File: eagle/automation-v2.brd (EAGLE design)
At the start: 65.8 x 104.1 mm, 96 parts, among them IC1 MEGA48/88/168-AU, IC2 DS2482-100S, IC3 DS2482-100S, IC4 78L33, K1 SRD-05VDC-SL-C, K2 SRD-05VDC-SL-C, K3 SRD-05VDC-SL-C, K4 SRD-05VDC-SL-C, Q1 BSS123, Q2 BSS123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

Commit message: Initial PCB trace
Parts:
- added C19, C20, C21: (no value), rcl:E5-10,5
- added R37, R38, R39: (no value), rcl:M1206
- JP2, JP3: device pinhead:1X02/90 -> pinhead:1X02
- moved JP1 31.5 mm to (6.35, 17.8)
- moved R8 30.8 mm to (5.71, 12.7)
- moved JP2 24.9 mm to (4.76, -4.45), turned to 180 degrees
- moved R23 23.4 mm to (30.5, 17.8), flipped to the top
- moved R18 23.4 mm to (41.6, -23.8), flipped to the bottom
- moved JP3 21.8 mm to (4.76, -8.89), turned to 180 degrees
- moved R22 21.1 mm to (28.6, 17.8), flipped to the top
- moved R21 21.0 mm to (23.2, -35.2), flipped to the bottom, turned to 0 degrees
- moved R36 20.3 mm to (12.7, -1.91), flipped to the bottom, turned to 270 degrees
- moved R24 19.9 mm to (41.6, -42.9), flipped to the bottom
- moved R27 19.0 mm to (23.2, -17.1), flipped to the bottom, turned to 0 degrees
- moved D2 18.4 mm to (41.6, -45.4), turned to 0 degrees
- moved D1 18.1 mm to (41.9, -26.4), turned to 0 degrees
- moved R16 17.2 mm to (47.0, -19.1), turned to 180 degrees
- moved R9 16.6 mm to (46.7, -38.1), turned to 180 degrees
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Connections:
- new net N$14: C19.+, K3.A2, R37.2
- new net N$63: C20.+, K2.A2, R38.1
- new net N$66: C21.+, K1.A2, R39.1
- net 12V: now also R37.1, R38.2, R39.2; no longer K1.A2, K2.A2, K3.A2
- net GND: now also C19.-, C20.-, C21.-
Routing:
- net 12V: track 0.00 -> 296.1 mm, vias 0 -> 5
- net GND: track 0.00 -> 218.0 mm, vias 0 -> 30
- net N$46: track 0.00 -> 131.9 mm, vias 0 -> 5
- net N$23: track 0.00 -> 115.9 mm, vias 0 -> 5
- net N$53: track 0.00 -> 109.7 mm, vias 0 -> 5
- net VDD: track 0.00 -> 86.0 mm, vias 0 -> 1
- net Z5V: track 0.00 -> 79.9 mm, vias 0 -> 2
- net N$24: track 0.00 -> 78.7 mm, vias 0 -> 3
- net N$2: track 0.00 -> 70.6 mm, vias 0 -> 3
- net N$12: track 0.00 -> 66.2 mm, vias 0 -> 2
- net N$13: track 0.00 -> 53.5 mm, vias 0 -> 3
- net VCC: track 0.00 -> 51.8 mm, vias 0 -> 2
- net N$1: track 0.00 -> 48.2 mm, vias 0 -> 3
- net N$14: track 0.00 -> 47.2 mm, vias 0 -> 2
- net N$40: track 0.00 -> 45.5 mm, vias 0 -> 2
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- added copper zone on layer 1, net GND
- added copper zone on layer 16, net GND
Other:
- board size 65.8 x 104.1 mm -> 67 x 104.4 mm

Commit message: updated PCB trace
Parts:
- moved R19 54.6 mm to (30.2, 12.7), flipped to the top, turned to 90 degrees
- moved R15 53.8 mm to (39.7, 12.7), flipped to the top, turned to 270 degrees
- moved R20 51.4 mm to (28.3, 12.7), flipped to the top, turned to 270 degrees
- moved R9 51.1 mm to (41.6, 12.7), flipped to the top, turned to 90 degrees
- moved D2 48.6 mm to (40.6, 3.17), flipped to the top, turned to 90 degrees
- moved Q3 47.3 mm to (29.2, 7.62), flipped to the top, turned to 180 degrees
- moved Q1 47.0 mm to (40.6, 7.62), flipped to the top, turned to 180 degrees
- moved R25 37.5 mm to (34.0, 12.7), flipped to the top, turned to 90 degrees
- moved D3 37.0 mm to (29.2, 3.17), flipped to the top, turned to 90 degrees
- moved R17 36.0 mm to (35.9, 12.7), flipped to the top, turned to 270 degrees
- moved R26 34.4 mm to (32.1, 12.7), flipped to the top, turned to 270 degrees
- moved R16 33.1 mm to (37.8, 12.7), flipped to the top, turned to 90 degrees
- moved D1 30.0 mm to (36.8, 3.17), flipped to the top, turned to 90 degrees
- moved Q4 29.6 mm to (33.0, 7.62), flipped to the top, turned to 180 degrees
- moved Q2 28.3 mm to (36.8, 7.62), flipped to the top, turned to 180 degrees
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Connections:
- net N$23: now also IC1.14; no longer IC1.11
- net N$24: now also IC1.13; no longer IC1.12
- net N$46: now also IC1.11; no longer IC1.13
- net N$53: now also IC1.12; no longer IC1.14
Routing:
- net GND: track 218.0 -> 0.00 mm, vias 30 -> 16
- net N$46: track 131.9 -> 10.9 mm, vias 5 -> 0
- net N$23: track 115.9 -> 16.9 mm, vias 5 -> 0
- net N$53: track 109.7 -> 11.1 mm, vias 5 -> 0
- net N$41: track 9.35 -> 83.9 mm
- net 12V: track 296.1 -> 223.4 mm, vias 5 -> 4
- net N$24: track 78.7 -> 14.0 mm, vias 3 -> 0
- net N$48: track 9.38 -> 69.2 mm, vias 0 -> 1
- net N$35: track 9.54 -> 52.4 mm, vias 0 -> 1
- net N$55: track 9.34 -> 45.3 mm, vias 0 -> 1
- net VDD: track 86.0 -> 57.7 mm, vias 1 -> 2
- net N$12: track 66.2 -> 43.4 mm, vias 2 -> 1
- net N$36: track 25.6 -> 3.18 mm, vias 3 -> 1
- net N$56: track 23.1 -> 3.18 mm
- net N$43: track 23.0 -> 3.18 mm
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
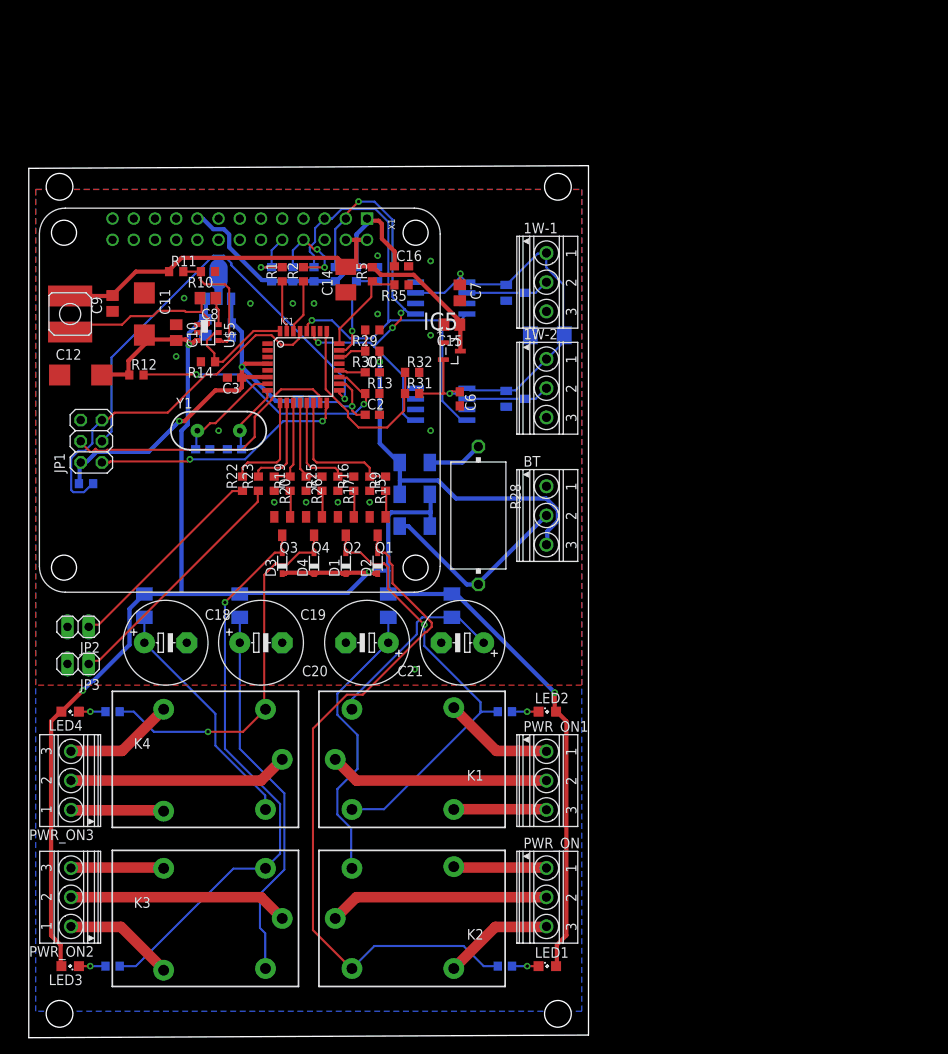
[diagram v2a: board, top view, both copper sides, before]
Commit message: RC version of PCB trace
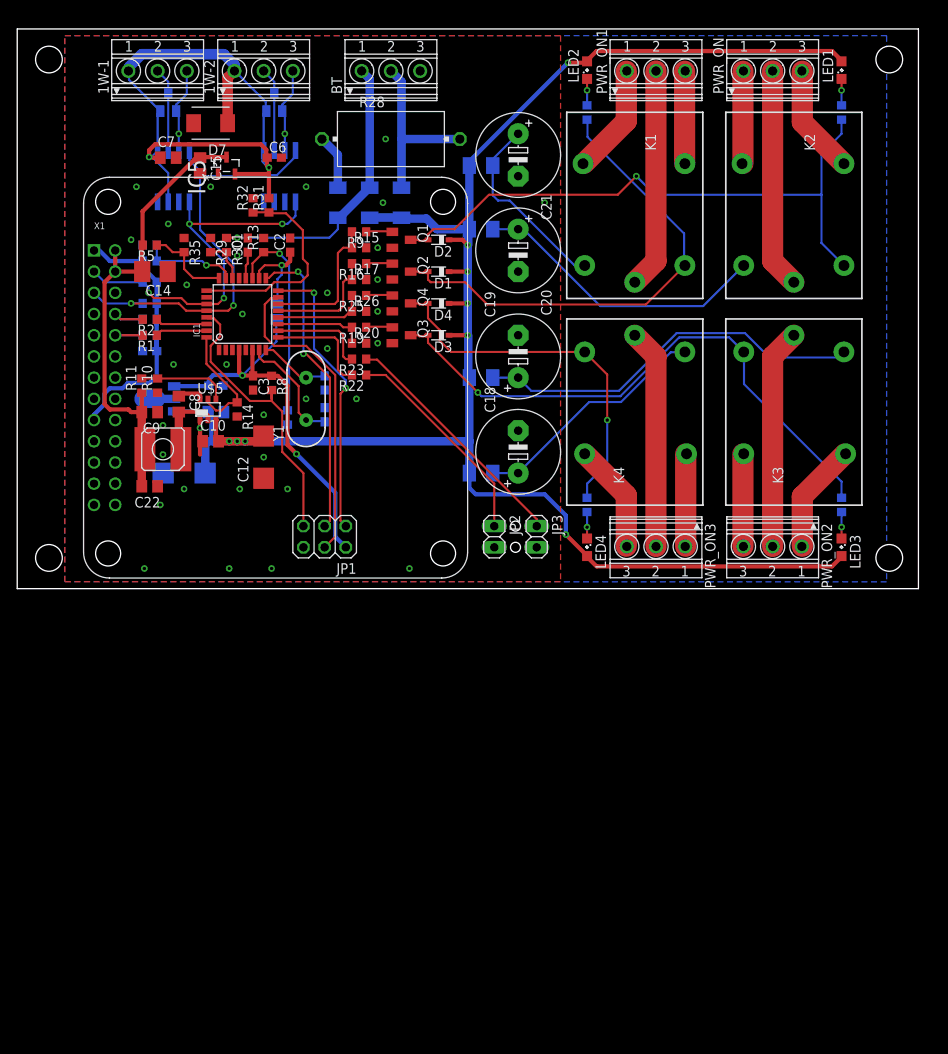
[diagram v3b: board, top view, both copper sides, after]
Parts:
- added C22: 0.1, rcl:C0805
- moved LED1 113.0 mm to (96.2, 62.2), turned to 90 degrees
- moved R24 109.9 mm to (96.2, 57.1), turned to 90 degrees
- moved LED3 105.1 mm to (96.2, 5.08), turned to 270 degrees
- moved R21 103.3 mm to (96.2, 10.2), turned to 270 degrees
- moved PWR_ON 102.7 mm to (87.9, 62.2), turned to 0 degrees
- moved K2 96.7 mm to (90.5, 45.7), turned to 270 degrees
- moved PWR_ON2 94.0 mm to (87.9, 5.08), turned to 180 degrees
- moved K3 92.9 mm to (90.5, 21.6), turned to 90 degrees
- moved PWR_ON1 86.1 mm to (74.0, 62.2), turned to 0 degrees
- moved LED2 77.0 mm to (65.7, 62.2), turned to 90 degrees
- moved PWR_ON3 75.5 mm to (74.0, 5.08), turned to 180 degrees
- moved R18 72.4 mm to (65.7, 57.1), turned to 90 degrees
- moved K1 71.3 mm to (71.4, 45.7), turned to 270 degrees
- moved K4 66.1 mm to (71.4, 21.6), turned to 90 degrees
- moved LED4 65.0 mm to (65.7, 5.08), turned to 270 degrees
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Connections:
- net GND: now also BT.3, C22.1; no longer BT.1
- net N$12: now also BT.1; no longer BT.3
- net Z5V: now also C22.2
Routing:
- net GND: track 0.00 -> 24.5 mm, vias 16 -> 36
- net VDD: track 57.7 -> 81.7 mm
- net N$19: track 53.4 -> 36.7 mm, vias 1 -> 2
- net N$3: track 22.3 -> 8.80 mm
- net N$41: track 83.9 -> 73.3 mm, vias 0 -> 1
- net N$2: track 63.3 -> 53.2 mm, vias 1 -> 2
- net N$25: track 34.2 -> 25.0 mm, vias 2 -> 1
- net N$12: track 43.4 -> 35.2 mm
- net N$13: track 43.0 -> 35.1 mm
- net N$35: track 52.4 -> 59.5 mm, vias 1 -> 0
- net N$1: track 52.6 -> 46.0 mm
- net 12V: track 223.4 -> 217.4 mm, vias 4 -> 9
- net N$8: track 11.1 -> 7.08 mm, vias 2 -> 0
- net N$22: track 14.5 -> 10.8 mm
- net N$20: track 30.9 -> 34.4 mm
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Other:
- board size 67 x 104.4 mm -> 107.9 x 67 mm

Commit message: Replace screw clamps
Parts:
- removed PWR_ON, PWR_ON1, PWR_ON2, PWR_ON3: 1751251, con-phoenix-350:1751251
- added X3, X4, X5, X6: (no value), con-wago-508:W237-133
- moved LED1 2.86 mm to (99.1, 62.2)
- moved LED3 2.86 mm to (99.1, 5.08)
- moved R21 2.86 mm to (99.1, 10.2)
- moved R24 2.86 mm to (99.1, 57.1)
- moved LED2 2.86 mm to (62.9, 62.2)
- moved LED4 2.86 mm to (62.9, 5.08)
- moved R18 2.86 mm to (62.9, 57.1)
- moved R27 2.86 mm to (62.9, 10.2)
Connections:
- net N$28: now also X4.2; no longer PWR_ON.2
- net N$32: now also X4.3; no longer PWR_ON.3
- net N$33: now also X4.1; no longer PWR_ON.1
- net N$42: now also X3.2; no longer PWR_ON1.2
- net N$44: now also X3.3; no longer PWR_ON1.3
- net N$45: now also X3.1; no longer PWR_ON1.1
- net N$50: now also X5.2; no longer PWR_ON2.2
- net N$51: now also X5.3; no longer PWR_ON2.3
- net N$52: now also X5.1; no longer PWR_ON2.1
- net N$57: now also X6.2; no longer PWR_ON3.2
- net N$58: now also X6.3; no longer PWR_ON3.3
- net N$59: now also X6.1; no longer PWR_ON3.1
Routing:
- net 12V: track 217.4 -> 234.6 mm
- net VDD: track 81.7 -> 76.0 mm
- net N$41: track 73.3 -> 76.6 mm
- net N$48: track 69.5 -> 71.3 mm
- net N$35: track 59.5 -> 61.2 mm
- net N$45: track 13.3 -> 11.7 mm
- net N$52: track 13.3 -> 11.7 mm
- net N$58: track 13.2 -> 11.7 mm
- net N$32: track 13.2 -> 11.7 mm
- net N$42: track 26.4 -> 25.5 mm
- net N$57: track 26.4 -> 25.5 mm
- net N$50: track 26.4 -> 25.5 mm
- net N$28: track 26.4 -> 25.5 mm
- net N$55: track 44.7 -> 45.5 mm
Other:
- board size 107.9 x 67 mm -> 109.5 x 67 mm

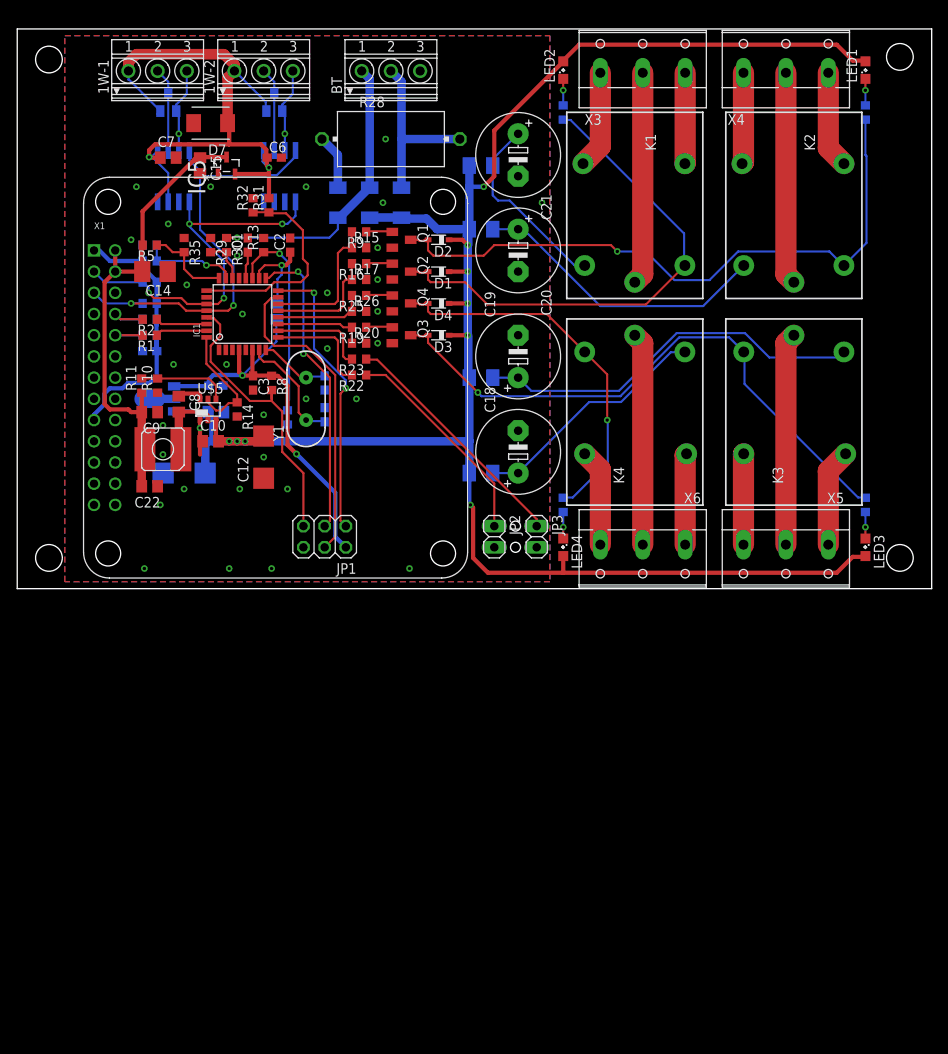
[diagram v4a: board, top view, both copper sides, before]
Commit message: changed Relay footprint
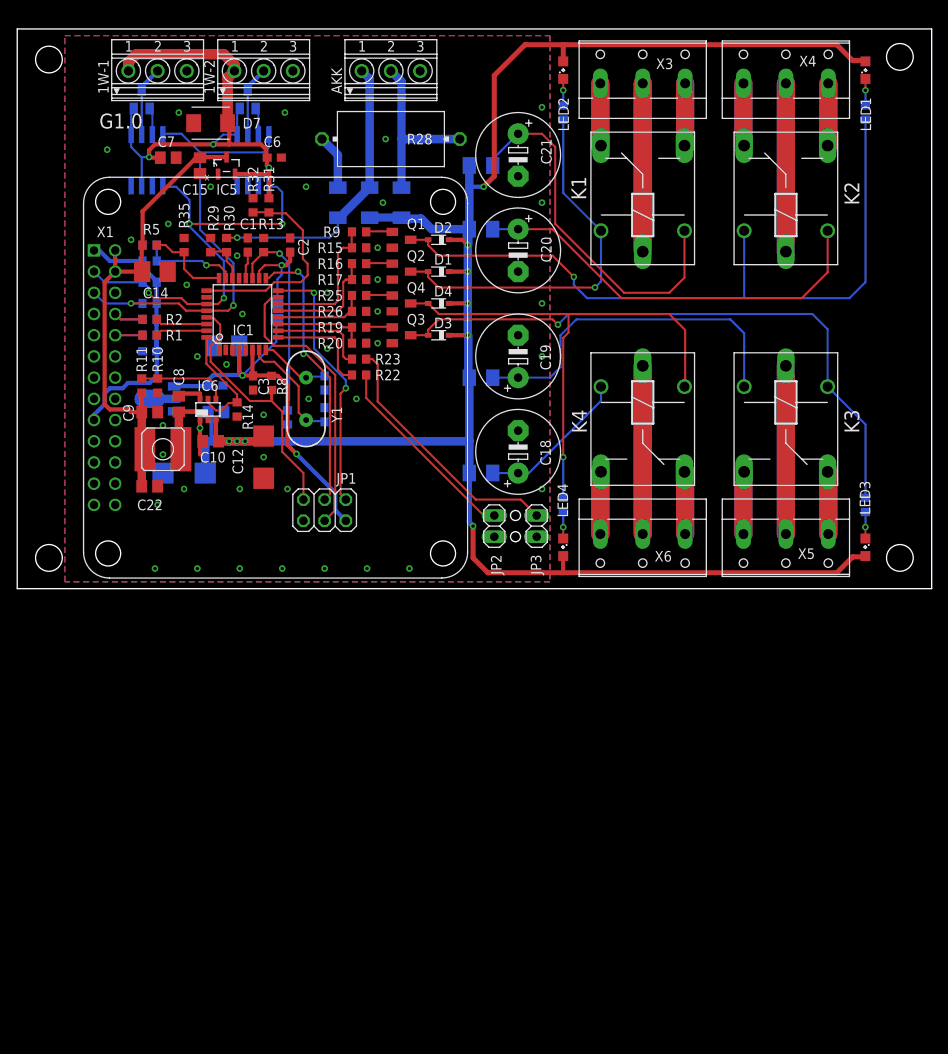
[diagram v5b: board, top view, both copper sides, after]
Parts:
- added C23: 47.0, rcl:B/3528-21R
- K1, K2, K3, K4: device relay:ZN5 -> relay:NRP18
- moved IC3 3.70 mm to (13.0, 51.4)
- moved IC2 3.70 mm to (25.7, 51.4)
- moved D9 3.19 mm to (25.1, 58.7)
- moved D8 3.19 mm to (12.4, 58.7)
- moved JP1 3.18 mm to (34.3, 9.53)
- moved K1 1.59 mm to (72.4, 47.0), turned to 90 degrees
- moved K2 1.59 mm to (89.5, 47.0), turned to 90 degrees
- moved K3 1.59 mm to (89.5, 20.3), turned to 270 degrees
- moved K4 1.59 mm to (72.4, 20.3), turned to 270 degrees
- moved JP2 1.27 mm to (54.6, 7.62)
- moved JP3 1.27 mm to (59.7, 7.62)
- moved X5 1.27 mm to (89.5, 6.03)
- moved X6 1.27 mm to (72.4, 6.03)
- moved X3 1.27 mm to (72.4, 61.3)
- moved X4 1.27 mm to (89.5, 61.3)
- renumbered BT to AKK, U$5 to IC6
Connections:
- net GND: now also C23.-
- net N$14: now also K3.2; no longer K3.A2
- net N$28: now also K2.P; no longer K2.11
- net N$32: now also K2.S; no longer K2.14
- net N$33: now also K2.O; no longer K2.12
- net N$35: now also K1.1; no longer K1.A1
- net N$41: now also K2.1; no longer K2.A1
- net N$42: now also K1.P; no longer K1.11
- net N$44: now also K1.S; no longer K1.14
- net N$45: now also K1.O; no longer K1.12
- net N$48: now also K3.1; no longer K3.A1
- net N$50: now also K3.P; no longer K3.11
- net N$51: now also K3.S; no longer K3.14
- net N$52: now also K3.O; no longer K3.12
- net N$55: now also K4.1; no longer K4.A1
- net N$57: now also K4.P; no longer K4.11
- net N$58: now also K4.S; no longer K4.14
- net N$59: now also K4.O; no longer K4.12
- net N$63: now also K2.2; no longer K2.A2
- net N$66: now also K1.2; no longer K1.A2
- net N$9: now also K4.2; no longer K4.A2
- net VCC: now also C23.+
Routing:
- net N$66: track 23.2 -> 44.7 mm
- net N$55: track 45.5 -> 63.4 mm
- net N$35: track 61.2 -> 45.5 mm, vias 0 -> 1
- net N$57: track 25.5 -> 40.5 mm
- net N$50: track 25.5 -> 40.5 mm
- net N$28: track 25.5 -> 40.5 mm
- net N$42: track 25.5 -> 40.2 mm
- net N$63: track 35.9 -> 49.8 mm
- net GND: track 24.5 -> 10.7 mm, vias 36 -> 43
- net N$9: track 29.0 -> 18.2 mm
- net N$41: track 76.6 -> 86.6 mm
- net VDD: track 76.0 -> 69.3 mm, vias 2 -> 3
- net N$1: track 46.0 -> 52.2 mm
- net 12V: track 234.6 -> 240.6 mm
- net N$14: track 47.1 -> 42.3 mm
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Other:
- board text added: "G1.0"
